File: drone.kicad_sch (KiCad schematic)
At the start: 49 parts, among them J2 Conn_01x02, J3 Conn_01x02, J4 Conn_01x02, J5 Conn_01x02, J6 Conn_01x02, J7 USB_B_Micro, Q1 Si2319CDS, Q2 Si2319CDS, Q3 Si2319CDS, Q4 Si2319CDS, Q5 BSS138, Q6 BSS138, U1 ESP32-WROOM-32, U2 MPU-6050, U3 DWM1000, U4 BMP280, U5 LM1117MP-3.3, U6 CH340C

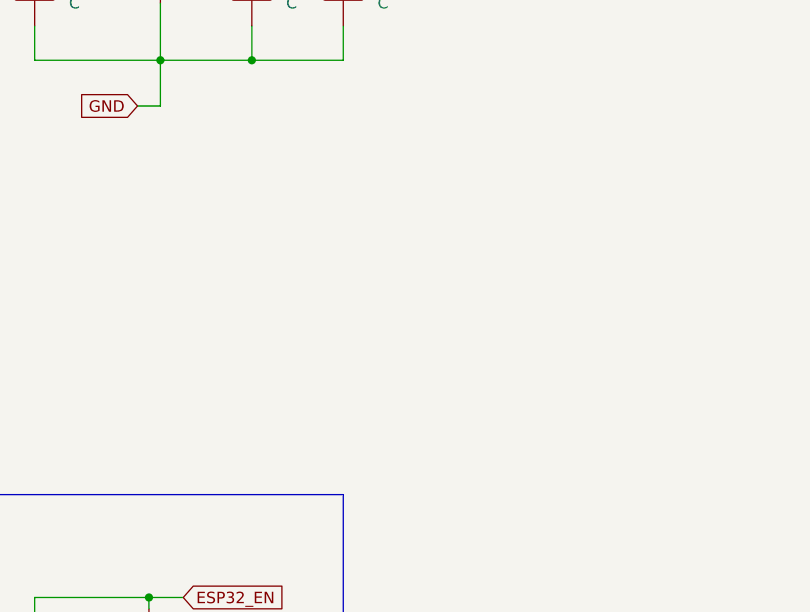
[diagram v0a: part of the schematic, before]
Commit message: add magnetometer + resive to max 10x10cm
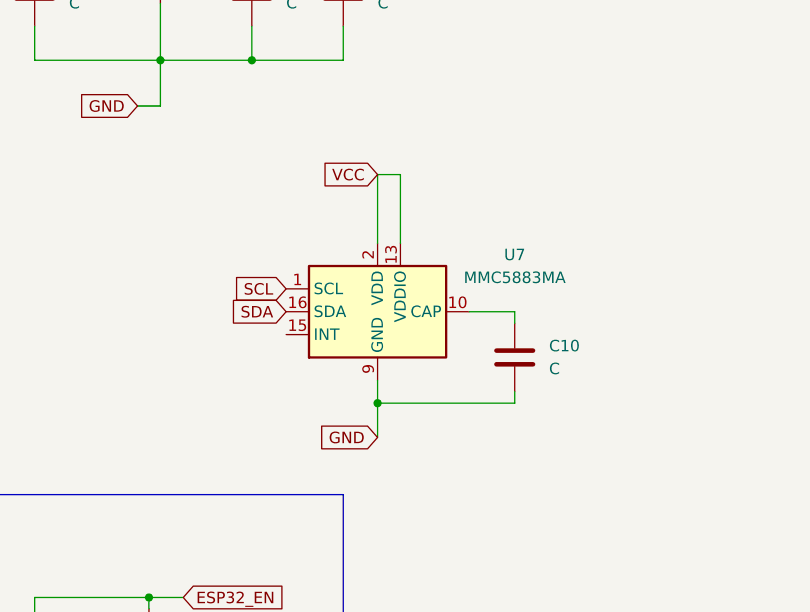
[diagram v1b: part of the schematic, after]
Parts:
- added C10: C, Capacitor_SMD:C_0603_1608Metric, symbol Device:C
- added U7: MMC5883MA, Package_LGA:LGA-16_3x3mm_P0.5mm, symbol Sensor_Magnetic:MMC5883MA
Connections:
- net GND: now also C10.2, U7.11 (GND), U7.9 (GND)
- net SCL: now also U7.1 (SCL)
- net SDA: now also U7.16 (SDA)
- net VCC: now also U7.13 (VDDIO), U7.2 (VDD)
- new net: C10.1, U7.10 (CAP)

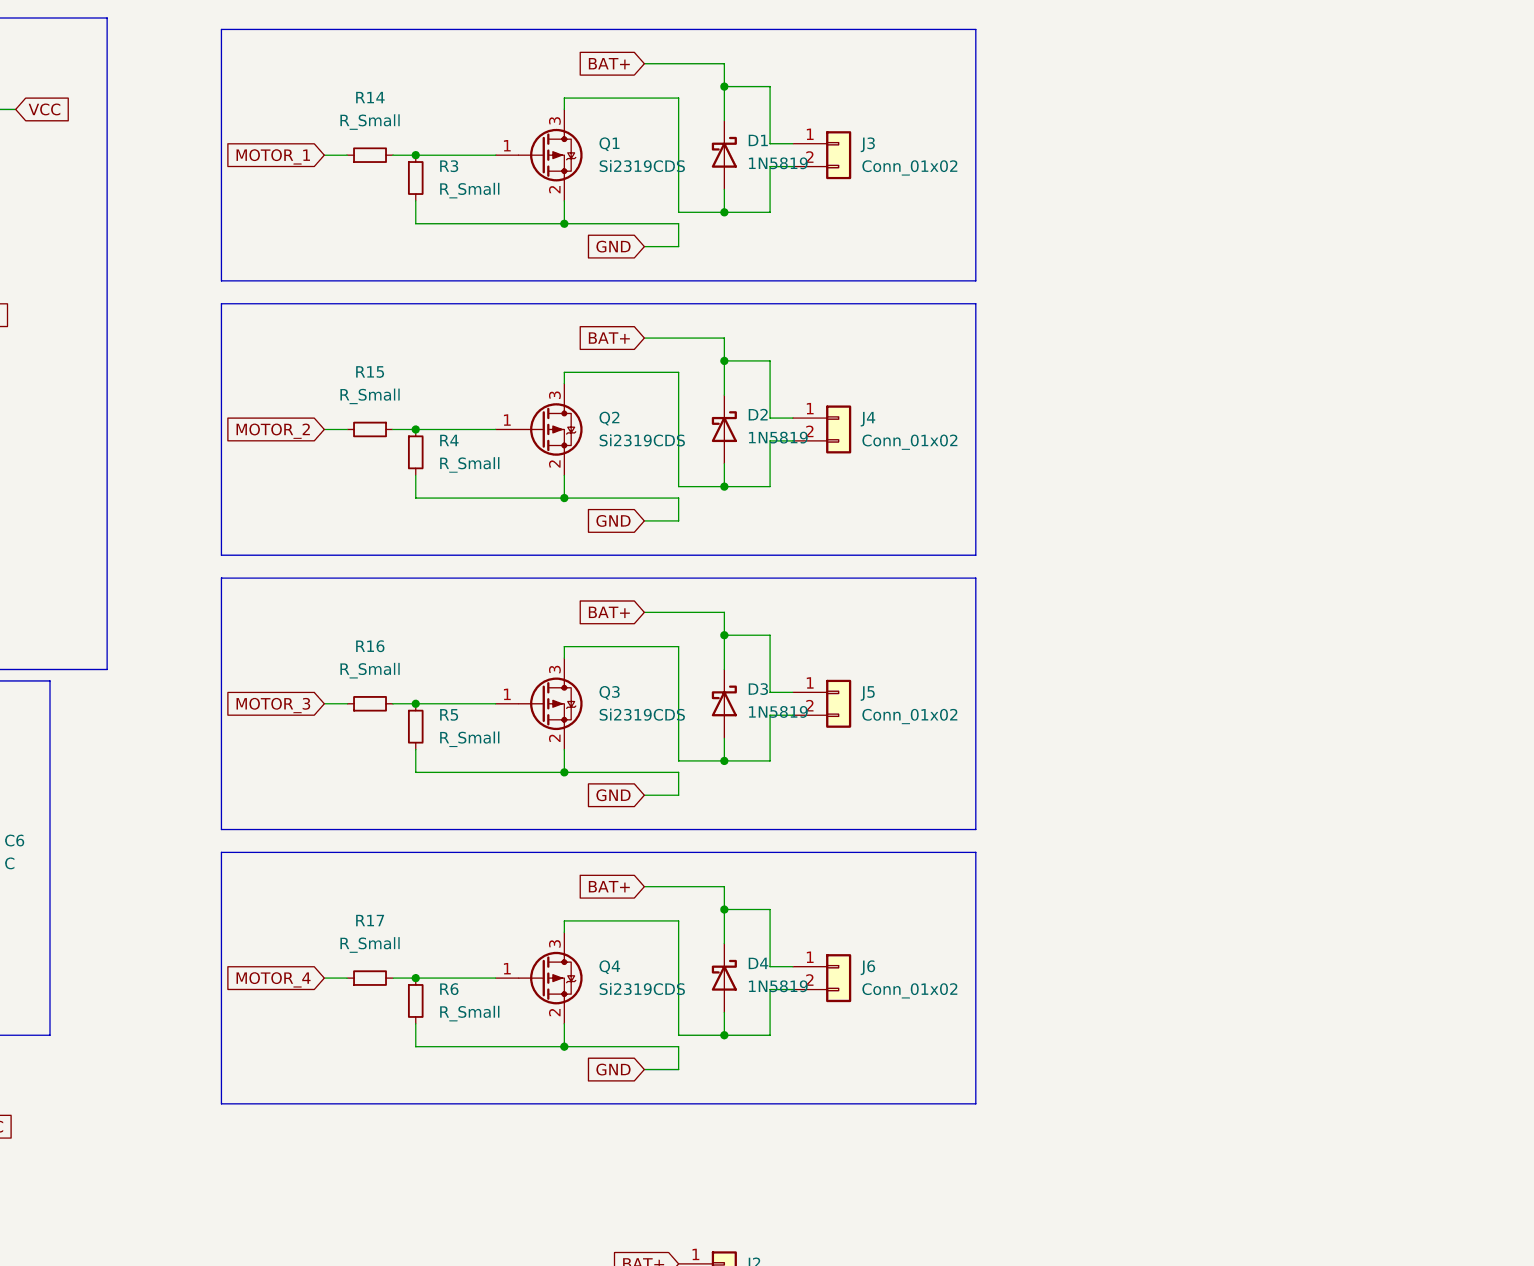
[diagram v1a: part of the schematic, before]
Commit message: pass si2301 to DRV8231
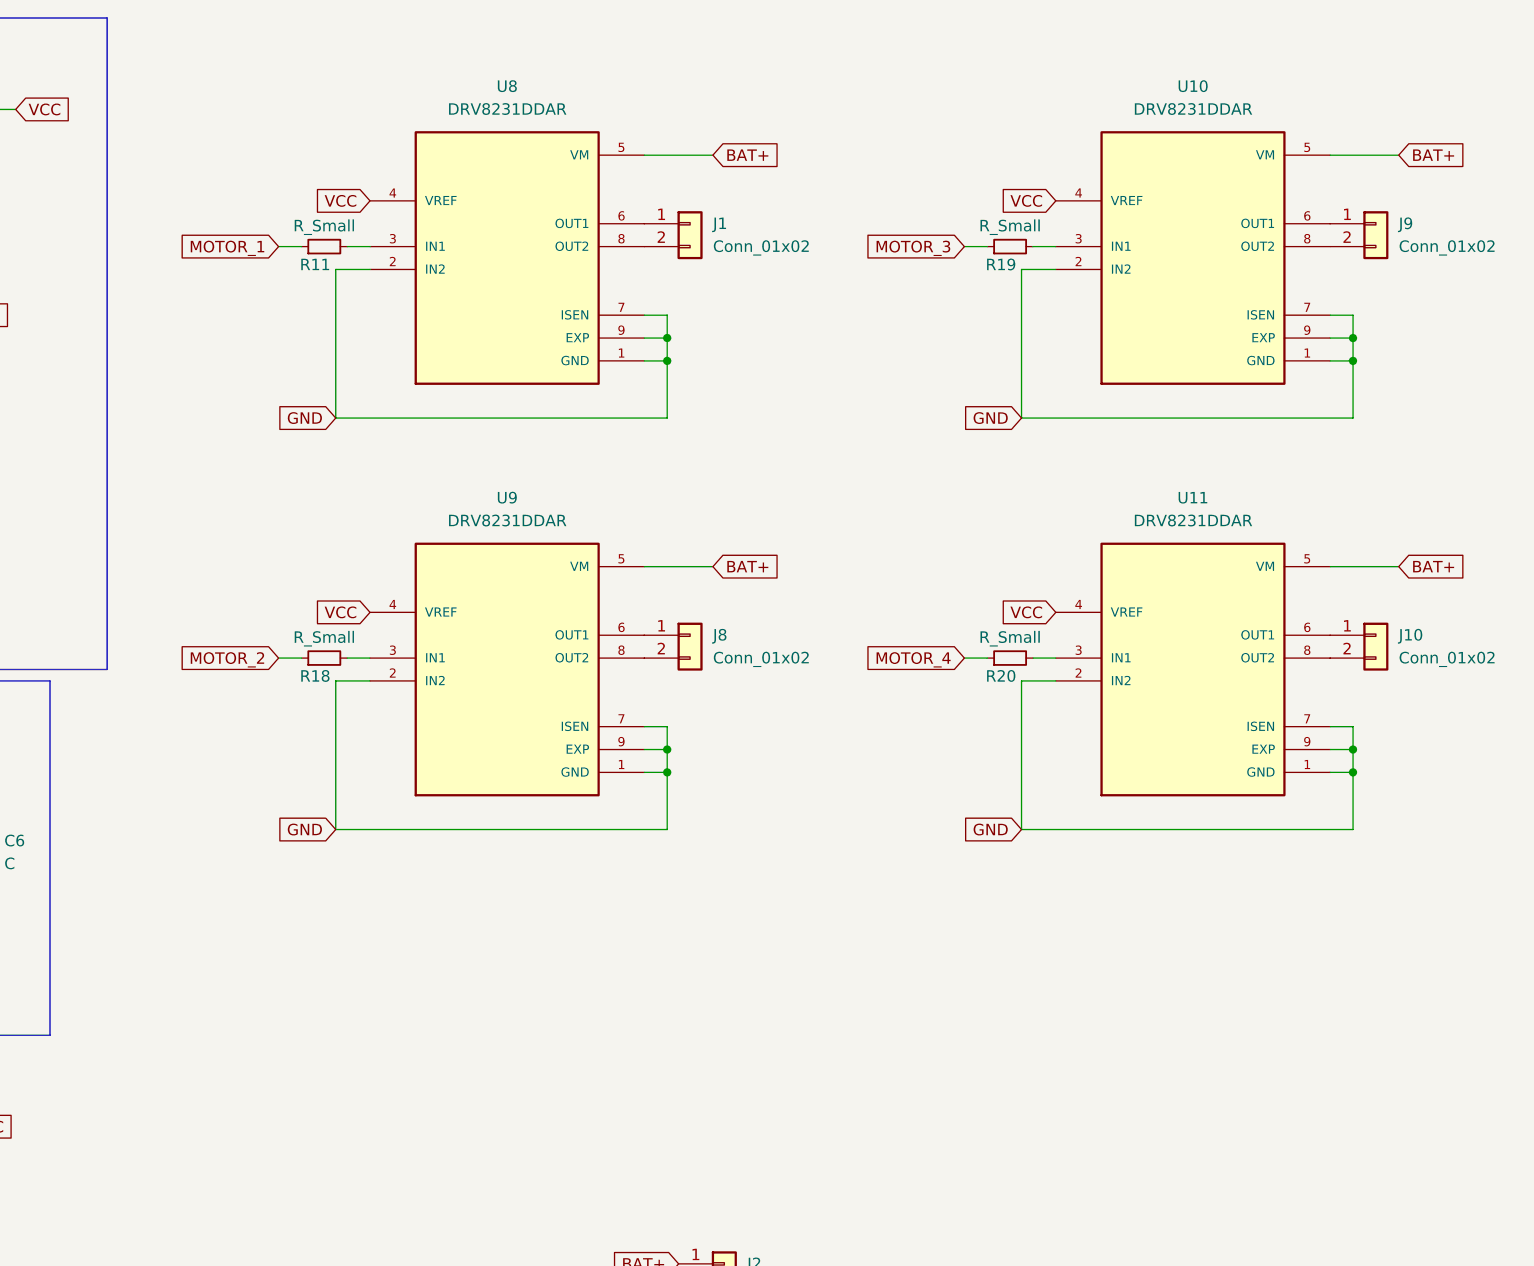
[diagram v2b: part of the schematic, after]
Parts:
- removed D1, D2, D3, D4: 1N5819, Diode_THT:D_DO-41_SOD81_P10.16mm_Horizontal, symbol Diode:1N5819
- removed J3, J4, J5, J6: Conn_01x02, Connector_PinHeader_2.54mm:PinHeader_1x02_P2.54mm_Vertical, symbol Connector_Generic:Conn_01x02
- removed Q1, Q2, Q3, Q4: Si2319CDS, Package_TO_SOT_SMD:SOT-23, symbol Transistor_FET:Si2319CDS
- removed R14, R15, R16, R17, R3, R4, R5, R6: R_Small, Resistor_SMD:R_0603_1608Metric, symbol Device:R_Small
- added J1, J10, J8, J9: Conn_01x02, Connector_PinHeader_2.54mm:PinHeader_1x02_P2.54mm_Vertical, symbol Connector_Generic:Conn_01x02
- added R11, R18, R19, R20: R_Small, Resistor_SMD:R_0603_1608Metric, symbol Device:R_Small
- added U10, U11, U8, U9: DRV8231DDAR, DRV8231:IC_DRV8231DDAR, symbol DRV8231:DRV8231DDAR
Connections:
- net BAT+: now also U10.5 (VM), U11.5 (VM), U8.5 (VM), U9.5 (VM)
- net GND: now also U10.1 (GND), U10.2 (IN2), U10.7 (ISEN), U10.9 (EXP), U11.1 (GND), U11.2 (IN2), U11.7 (ISEN), U11.9 (EXP), U8.1 (GND), U8.2 (IN2), U8.7 (ISEN), U8.9 (EXP), U9.1 (GND), U9.2 (IN2), U9.7 (ISEN), U9.9 (EXP)
- net MOTOR_1: now also R11.1
- net MOTOR_2: now also R18.1
- net MOTOR_3: now also R19.1
- net MOTOR_4: now also R20.1
- net VCC: now also U10.4 (VREF), U11.4 (VREF), U8.4 (VREF), U9.4 (VREF)
- new net: R18.2, U9.3 (IN1)
- new net: J8.1 (Pin_1), U9.6 (OUT1)
- new net: J8.2 (Pin_2), U9.8 (OUT2)
- new net: R19.2, U10.3 (IN1)
- new net: J9.1 (Pin_1), U10.6 (OUT1)
- new net: J9.2 (Pin_2), U10.8 (OUT2)
- new net: R11.2, U8.3 (IN1)
- new net: J1.1 (Pin_1), U8.6 (OUT1)
- new net: J1.2 (Pin_2), U8.8 (OUT2)
- new net: J10.1 (Pin_1), U11.6 (OUT1)
- new net: J10.2 (Pin_2), U11.8 (OUT2)
- new net: R20.2, U11.3 (IN1)

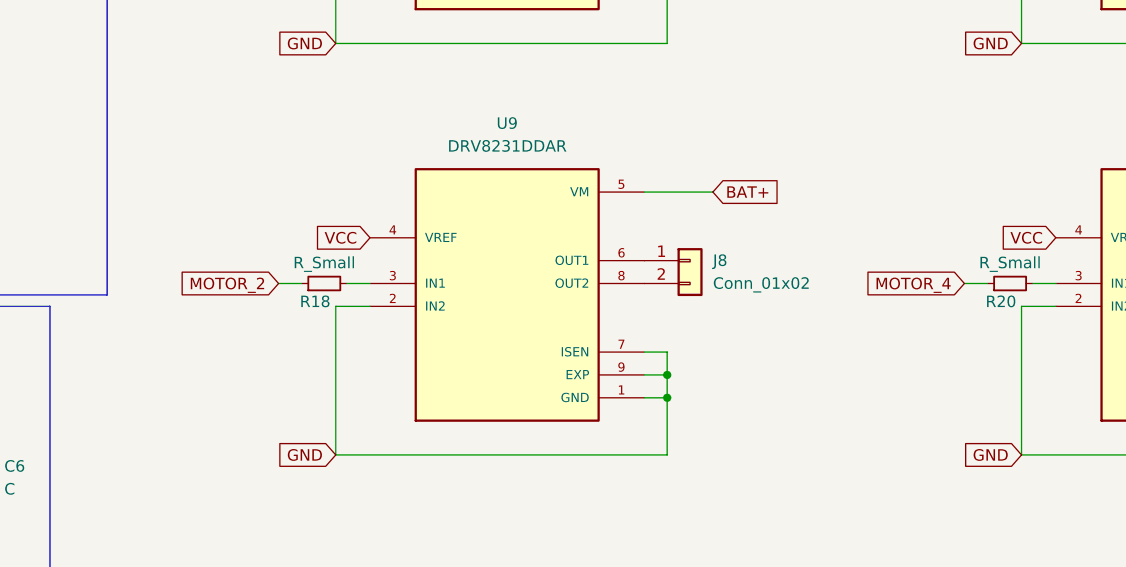
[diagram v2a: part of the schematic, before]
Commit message: add motor driver wiring on pcb
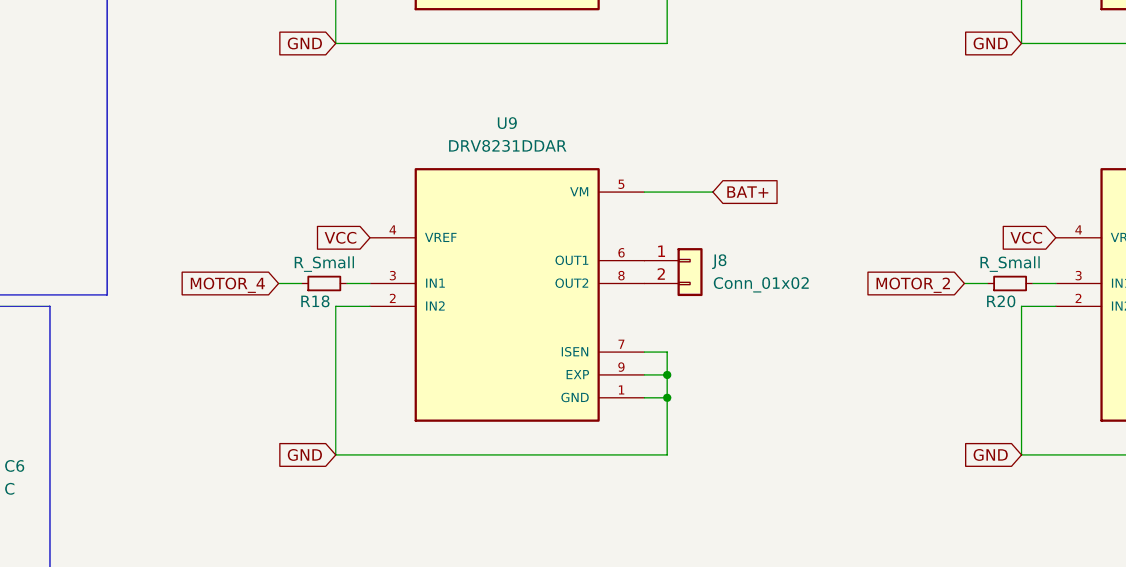
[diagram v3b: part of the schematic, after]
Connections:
- net MOTOR_2: now also R20.1; no longer R18.1
- net MOTOR_4: now also R18.1; no longer R20.1
